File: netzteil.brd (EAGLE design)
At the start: 50 x 80 mm, 56 parts, among them M1 STL100NH3LL, M2 STL100NH3LL, M3 STL100NH3LL, M4 STL100NH3LL, X1 NEB21R

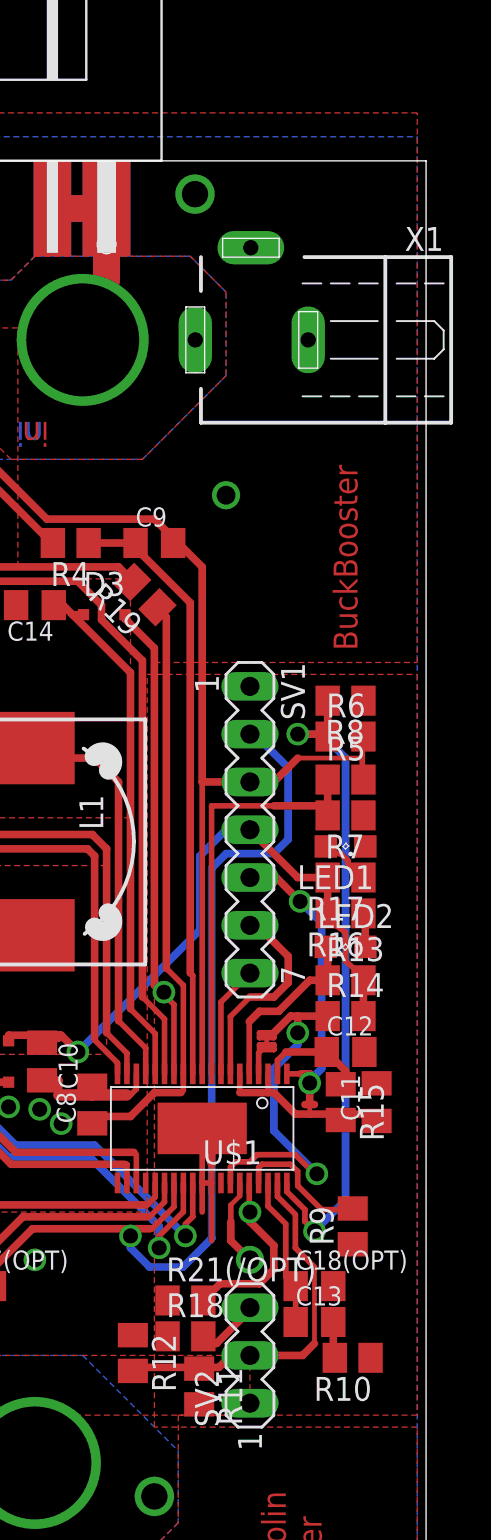
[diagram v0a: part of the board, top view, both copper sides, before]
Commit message: enable/undervoltage on pin header
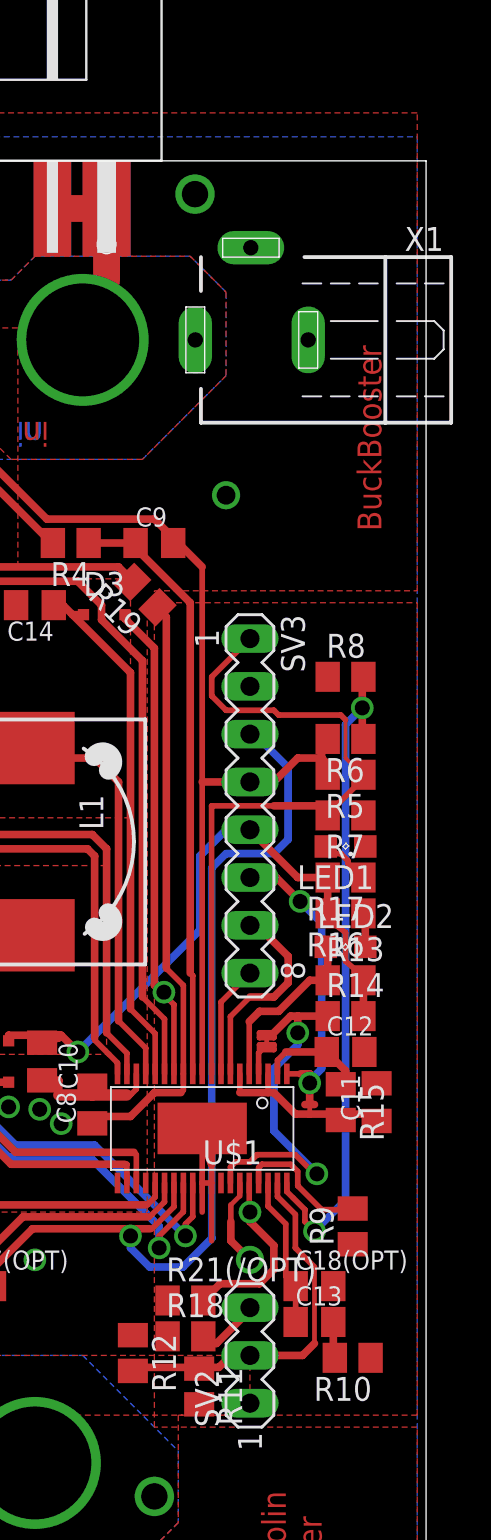
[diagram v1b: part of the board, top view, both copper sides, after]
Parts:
- removed SV1: (no value), con-lstb:MA07-1
- added SV3: (no value), con-lstb:MA08-1
- moved R8 1.27 mm to (45.7, 52.6), turned to 0 degrees
- moved R5 0.25 mm to (45.7, 47.4), turned to 180 degrees
- moved R6 0.13 mm to (45.7, 49.3), turned to 180 degrees
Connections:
- net +12V: now also SV3.3; no longer SV1.2
- net +24V: now also SV3.4; no longer SV1.3
- net +5V: now also SV3.5; no longer SV1.4
- net GNDA: now also SV3.2; no longer SV1.1
- net N$13: now also SV3.1
- net N$2: now also SV3.7; no longer SV1.6
- net N$25: now also SV3.6; no longer SV1.5
- net N$3: now also SV3.8; no longer SV1.7
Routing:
- net N$13: track 22.5 -> 38.6 mm
- net +24V: track 69.1 -> 66.8 mm
